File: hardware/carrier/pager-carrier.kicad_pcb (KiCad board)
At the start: 2 copper layers, 38.9 x 48.9 mm, 79 parts, among them J1 PANEL, J2 CARDKB, J3 HAPTIC, J4 EXT_LED, J5 PIEZ, J6 TYPE-C 16PLT-H6.5, J7 BATTERY, J8 FRONTLIGHT, M1 Walter, Q1 UMH3N, Q2 SI1308EDL, Q3 MMST3904, Q4 AO3401A, SW1 KMR221GLFS, SW2 MSS12C02LS-HB2.0, U1 CP2102N-A02-GQFN24, U2 SN74LVC2G126DCUR, U3 DRV2605LDGSR, U4 LIS2DW12TR, U5 BQ25185DLHR, U6 MAX17048G+T10, U7 TPS62840DLCR

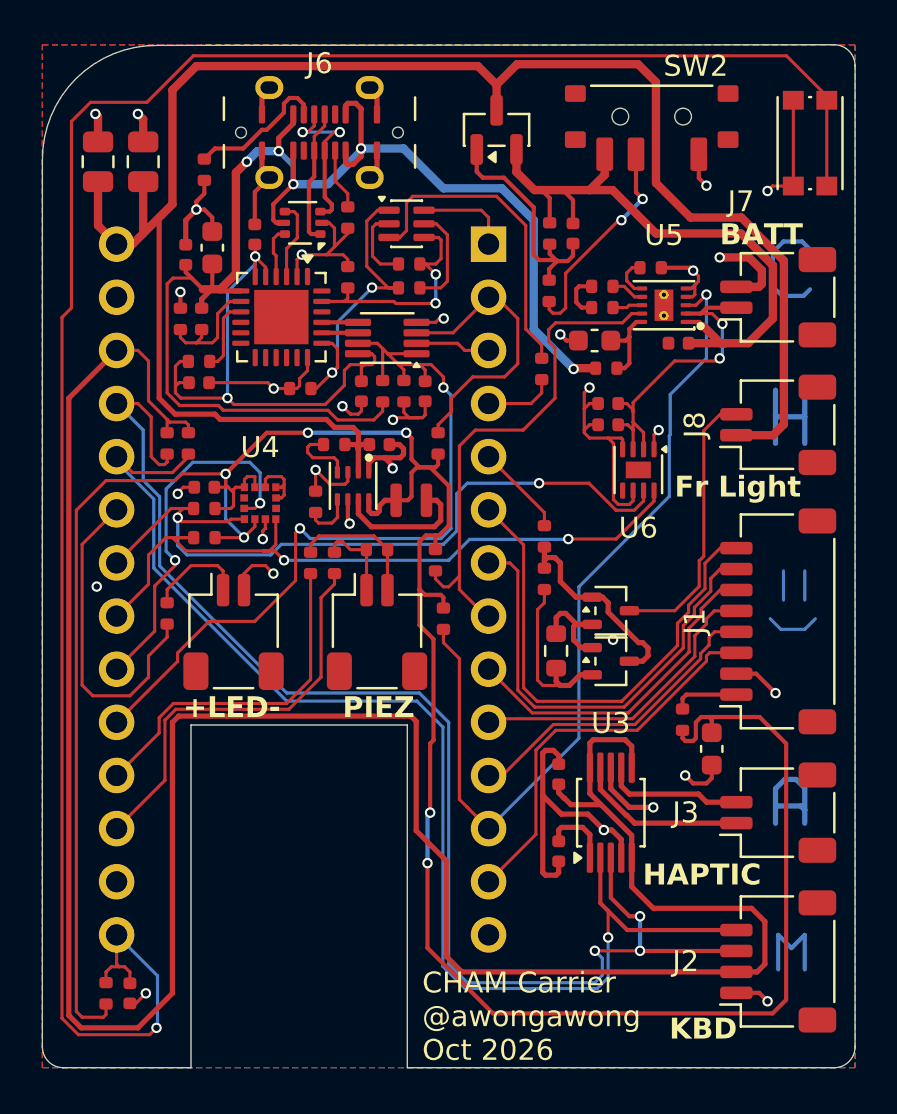
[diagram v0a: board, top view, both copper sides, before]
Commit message: Carrier: accelerometer -> MSKSEMI LIS2DW12TR-MS for Economic PCBA, JLC production files
U4 ST LIS2DW12TR (C189624, JLC "Standard Only") -> MSKSEMI LIS2DW12TR-MS
(C50385411, Economic and Standard). Same LGA-12 2x2 land pattern and pin-1
corner, different pinout (new project symbol); owner rerouted U4. The part is
an SC7A20-class die: WHO_AM_I 0x11, LIS3DH-style registers, I2C 0x18 with
SDO/SA0 low. Firmware follow-ups: accept 0x11, set SDO_PU in reg 0x57.

Also adds the ShouHan J6/SW2 footprints from the stock-part swap, the
Fabrication Toolkit options and production outputs (carrier and panel), and
the panel STEP. DRC 0 errors / 0 unconnected; ERC unchanged vs HEAD.

Co-Authored-By: Claude Opus 5.5 <noreply@anthropic.com>
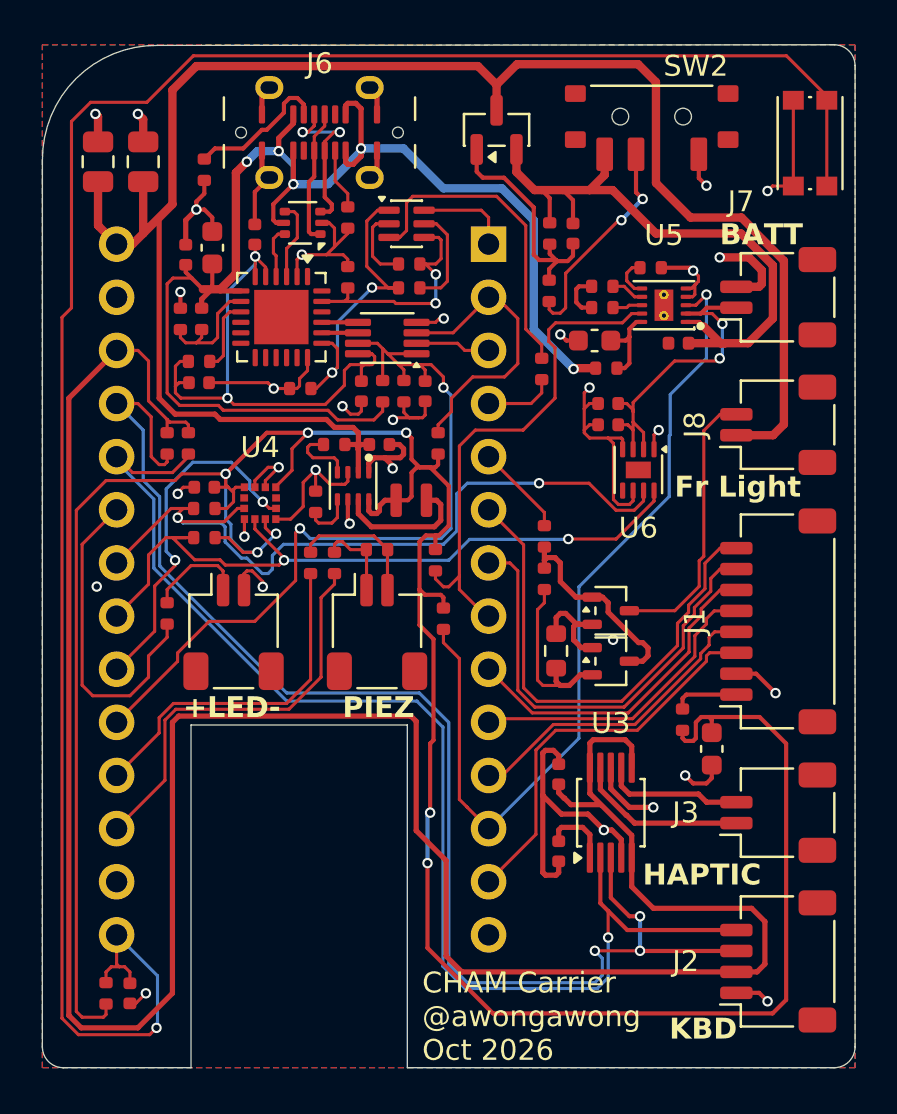
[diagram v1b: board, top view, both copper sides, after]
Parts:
- U4: value LIS2DW12TR -> LIS2DW12TR-MS
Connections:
- U4 pad 1: AON_SCL -> GND
- U4 pad 12: /Core/ACC_INT1 -> AON_SCL
- U4 pad 2: 3V3 -> AON_SDA
- U4 pad 3: GND -> 3V3
- U4 pad 4: AON_SDA -> GND
- U4 pad 5: unconnected-(U4-NC-Pad5) -> /Core/ACC_INT1
- U4 pad 6: GND -> unconnected-(U4-INT2-Pad6)
- U4 pad 7: GND -> 3V3
- U4 pad 9: 3V3 -> GND
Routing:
- net (no net): track 29.6 -> 0.00 mm
- net 3V3: track 128.5 -> 133.7 mm, vias 6 -> 7
- net GND: track 113.8 -> 116.7 mm, vias 30 -> 31
- net AON_SCL: track 36.1 -> 37.1 mm
- net AON_SDA: track 33.8 -> 34.6 mm
- net /Core/ACC_INT1: track 17.5 -> 16.9 mm
